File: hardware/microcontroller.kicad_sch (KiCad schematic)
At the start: 19 parts, among them U1 STM32G474QBT6

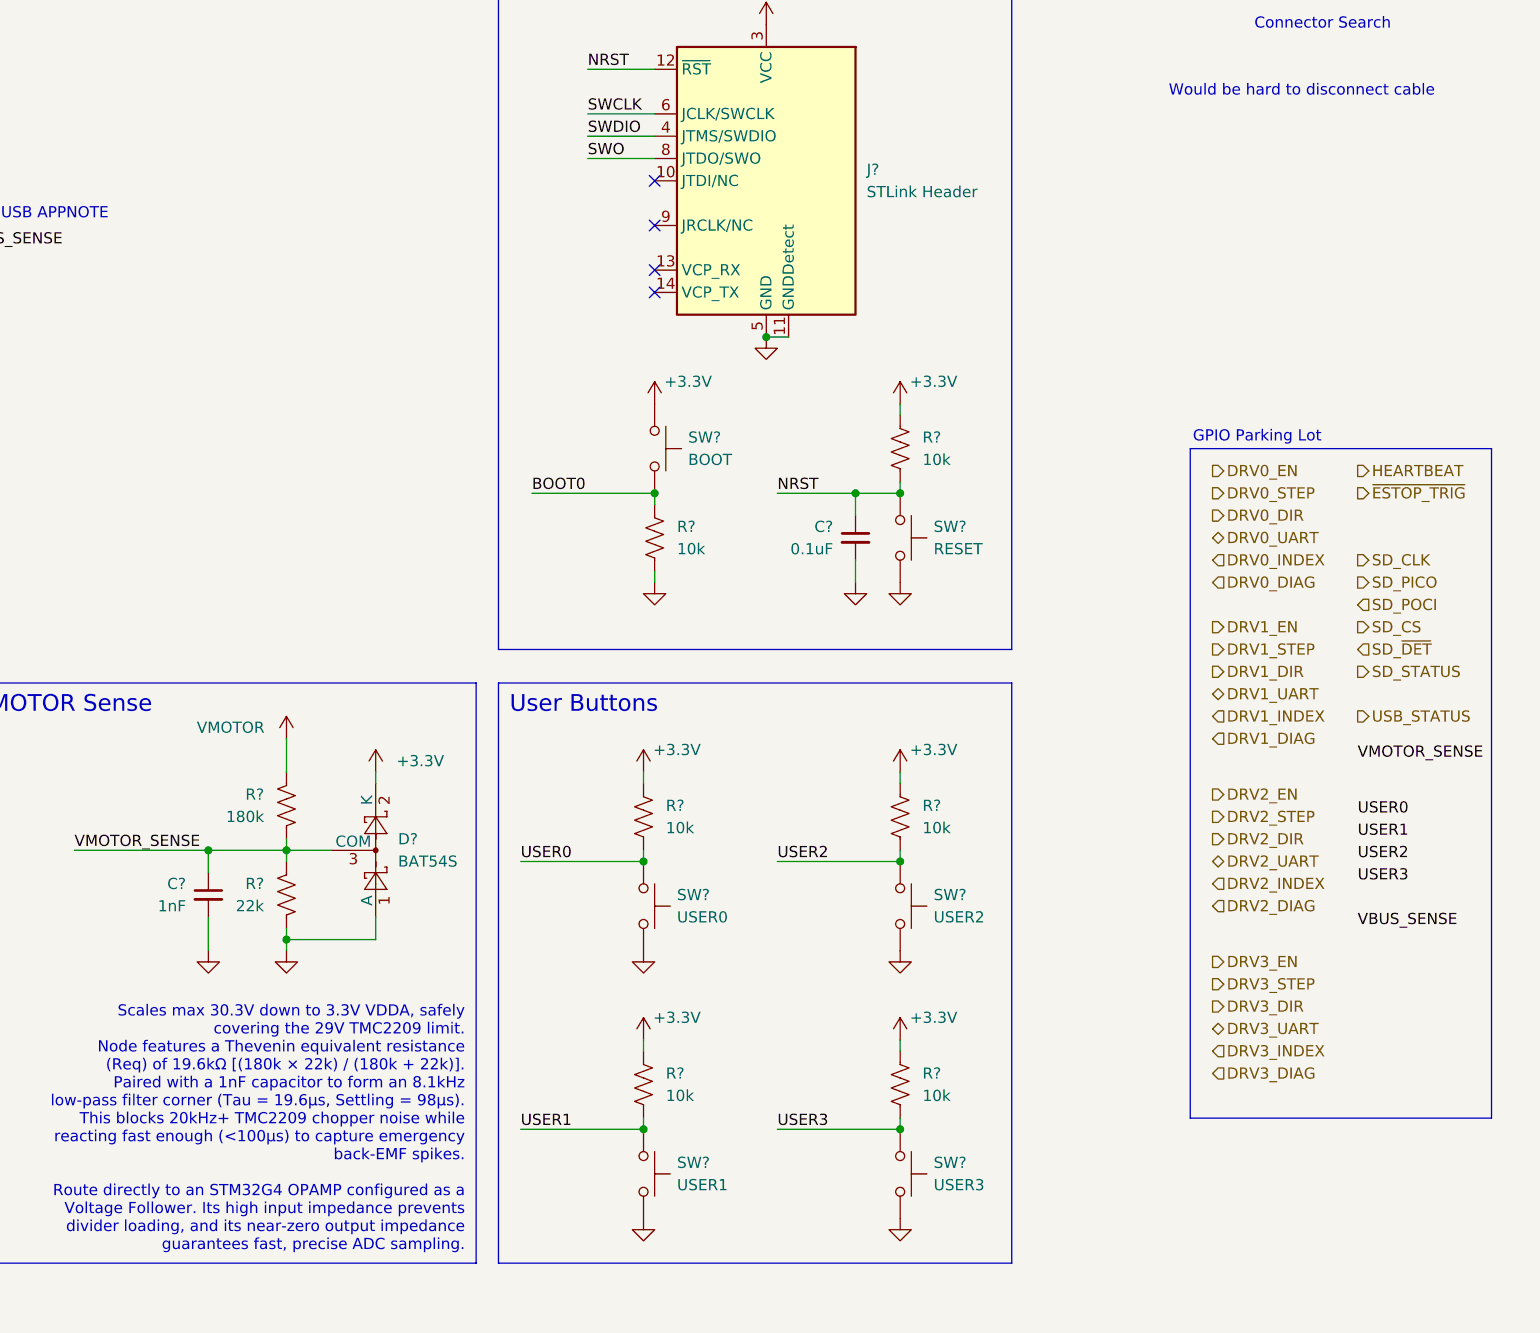
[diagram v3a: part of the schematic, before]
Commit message: Add QSPI Flash
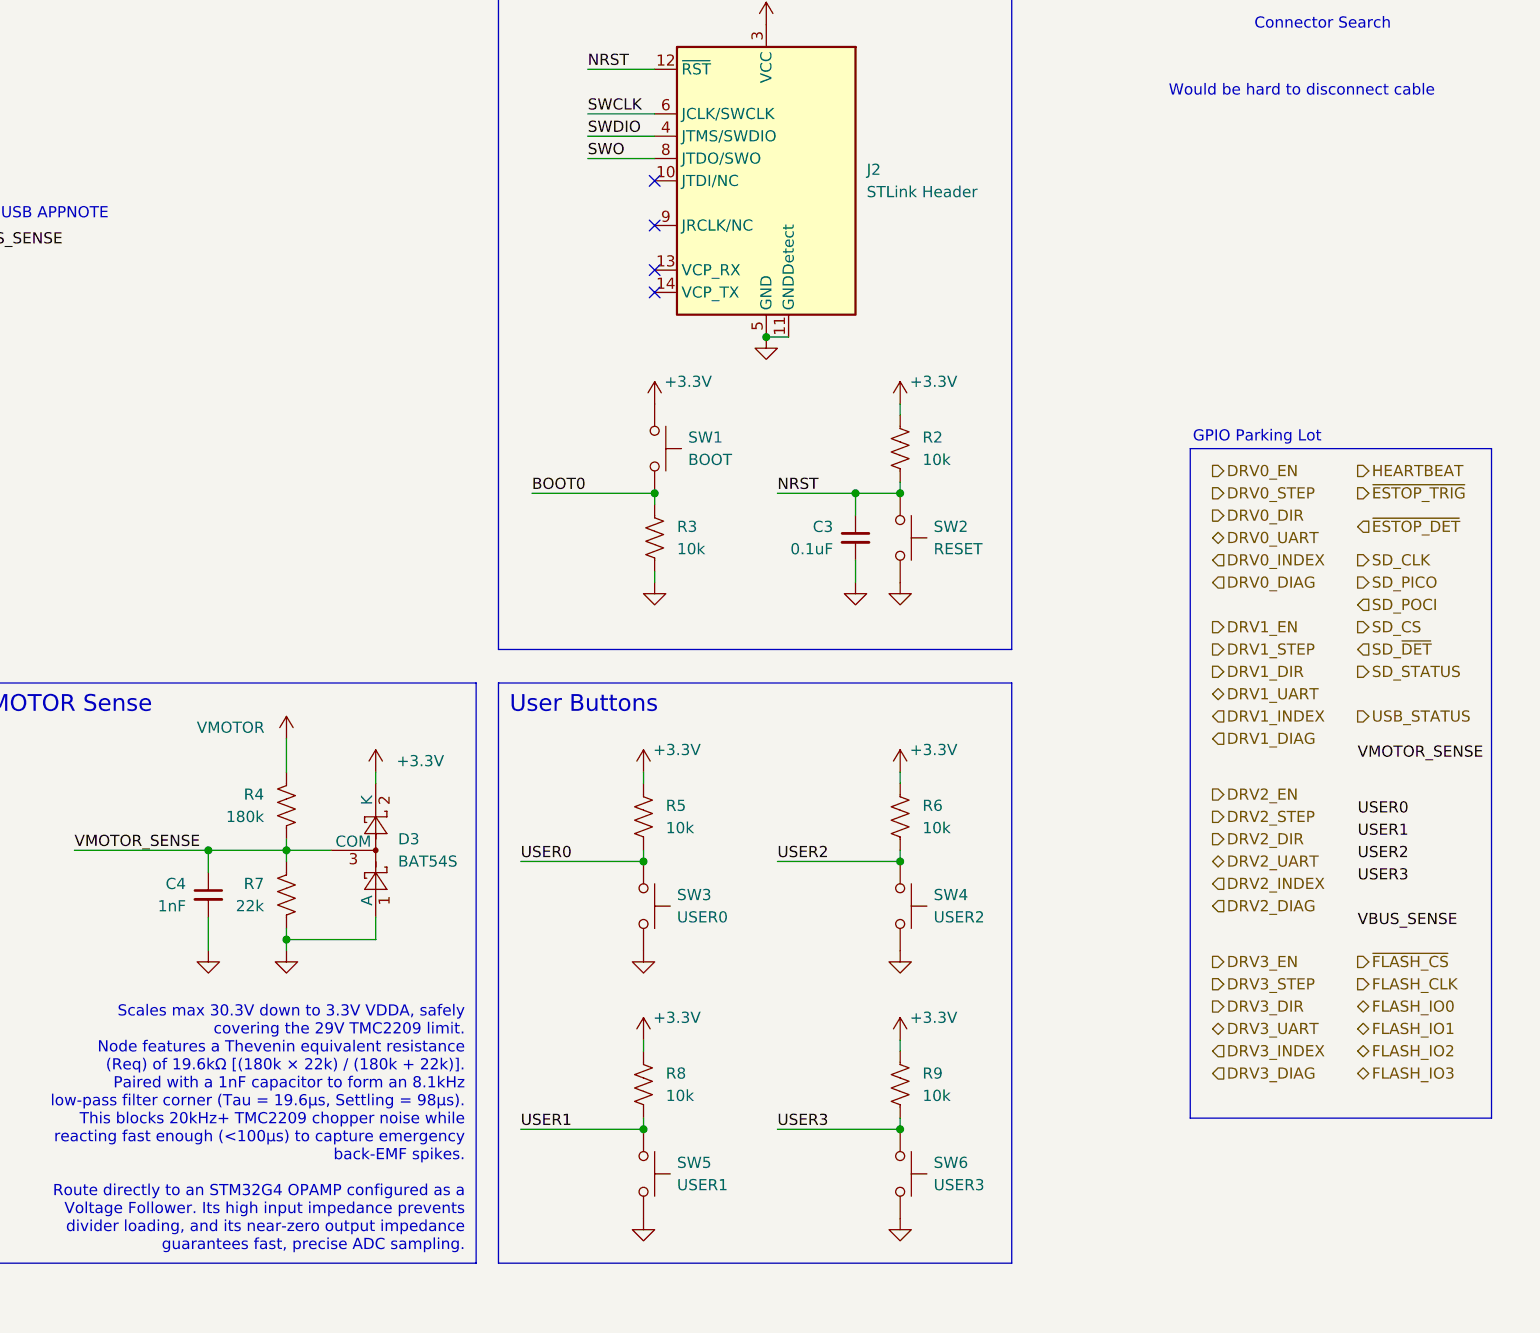
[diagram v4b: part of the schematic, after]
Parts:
- gave numbers to parts that had none: 18
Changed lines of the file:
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@@
 		)
 	)
+	(hierarchical_label "FLASH_CLK"
+		(shape output)
+		(at 303.53 137.16 0)
+		(fields_autoplaced yes)
+		(effects
+			(font
+				(size 1.27 1.27)
+			)
+			(justify left)
+		)
+		(property "GPIO Type" "QSPI"
+			(at 303.53 138.43 0)
+			(show_name no)
+			(do_not_autoplace no)
+			(effects
+				(font
+					(size 1.27 1.27)
+					(italic yes)
+				)
+				(justify left)
+			)
+		)
+	)
 	(hierarchical_label "DRV3_DIAG"
 		(shape input)
@@
 		)
 	)
+	(hierarchical_label "FLASH_IO2"
+		(shape bidirectional)
+		(at 303.53 144.78 0)
+		(fields_autoplaced yes)
+		(effects
+			(font
+				(size 1.27 1.27)
+			)
+			(justify left)
+		)
+		(property "GPIO Type" "QSPI"
+			(at 303.53 146.05 0)
+			(show_name no)
+			(do_not_autoplace no)
+			(effects
+				(font
+					(size 1.27 1.27)
+					(italic yes)
+				)
+				(justify left)
+			)
+		)
+	)
 	(hierarchical_label "DRV1_DIAG"
 		(shape input)
@@
 		)
 	)
+	(hierarchical_label "~{ESTOP_DET}"
+		(shape input)
+		(at 303.53 85.09 0)
+		(effects
+			(font
+				(size 1.27 1.27)
+			)
+			(justify left)
+		)
+	)
 	(hierarchical_label "USB_DP"
 		(shape input)
@@
 		)
 	)
+	(hierarchical_label "FLASH_IO0"
+		(shape bidirectional)
+		(at 303.53 139.7 0)
+		(fields_autoplaced yes)
+		(effects
+			(font
+				(size 1.27 1.27)
+			)
+			(justify left)
+		)
+		(property "GPIO Type" "QSPI"
+			(at 303.53 140.97 0)
+			(show_name no)
+			(do_not_autoplace no)
+			(effects
+				(font
+					(size 1.27 1.27)
+					(italic yes)
+				)
+				(justify left)
+			)
+		)
+	)
 	(hierarchical_label "DRV1_STEP"
 		(shape output)
@@
 		)
 	)
+	(hierarchical_label "FLASH_IO1"
+		(shape bidirectional)
+		(at 303.53 142.24 0)
+		(fields_autoplaced yes)
+		(effects
+			(font
+				(size 1.27 1.27)
+			)
+			(justify left)
+		)
+		(property "GPIO Type" "QSPI"
+			(at 303.53 143.51 0)
+			(show_name no)
+			(do_not_autoplace no)
+			(effects
+				(font
+					(size 1.27 1.27)
+					(italic yes)
+				)
+				(justify left)
+			)
+		)
+	)
 	(hierarchical_label "DRV3_DIR"
 		(shape output)
@@
 		)
 	)
+	(hierarchical_label "FLASH_IO3"
+		(shape bidirectional)
+		(at 303.53 147.32 0)
+		(fields_autoplaced yes)
+		(effects
+			(font
+				(size 1.27 1.27)
+			)
+			(justify left)
+		)
+		(property "GPIO Type" "QSPI"
+			(at 303.53 148.59 0)
+			(show_name no)
+			(do_not_autoplace no)
+			(effects
+				(font
+					(size 1.27 1.27)
+					(italic yes)
+				)
+				(justify left)
+			)
+		)
+	)
 	(hierarchical_label "DRV1_DIR"
 		(shape output)
@@
 		)
 	)
+	(hierarchical_label "~{FLASH_CS}"
+		(shape output)
+		(at 303.53 134.62 0)
+		(effects
+			(font
+				(size 1.27 1.27)
+			)
+			(justify left)
+		)
+	)
 	(hierarchical_label "SD_CS"
 		(shape output)
@@
 		(in_pos_files yes)
 		(dnp no)
-		(property "Reference" "C?"
+		(property "Reference" "C4"
 			(at 170.18 125.7362 0)
 			(show_name no)
@@
 			(project "stepping-stone"
 				(path "/793a882e-3f7b-468b-a863-41a1f527e1bf/d2f9d032-a5e5-45d0-b37f-4be86e3babb1"
-					(reference "C?")
+					(reference "C4")
 					(unit 1)
 				)
@@
 		(dnp no)
 		(fields_autoplaced yes)
-		(property "Reference" "R?"
+		(property "Reference" "R5"
 			(at 224.79 116.8399 0)
 			(show_name no)
@@
 			(project "stepping-stone"
 				(path "/793a882e-3f7b-468b-a863-41a1f527e1bf/d2f9d032-a5e5-45d0-b37f-4be86e3babb1"
-					(reference "R?")
+					(reference "R5")
 					(unit 1)
 				)
@@
 		(in_pos_files yes)
 		(dnp no)
-		(property "Reference" "R?"
+		(property "Reference" "R4"
 			(at 179.07 115.5699 0)
 			(show_name no)
@@
 			(project "stepping-stone"
 				(path "/793a882e-3f7b-468b-a863-41a1f527e1bf/d2f9d032-a5e5-45d0-b37f-4be86e3babb1"
-					(reference "R?")
+					(reference "R4")
 					(unit 1)
 				)
@@
 		(dnp no)
 		(fields_autoplaced yes)
-		(property "Reference" "R?"
+		(property "Reference" "R6"
 			(at 254 116.8399 0)
 			(show_name no)
@@
 			(project "stepping-stone"
 				(path "/793a882e-3f7b-468b-a863-41a1f527e1bf/d2f9d032-a5e5-45d0-b37f-4be86e3babb1"
-					(reference "R?")
+					(reference "R6")
 					(unit 1)
 				)
@@
 		(in_pos_files yes)
 		(dnp no)
-		(property "Reference" "R?"
+		(property "Reference" "R7"
 			(at 179.07 125.7299 0)
 			(show_name no)
@@
 			(project "stepping-stone"
 				(path "/793a882e-3f7b-468b-a863-41a1f527e1bf/d2f9d032-a5e5-45d0-b37f-4be86e3babb1"
-					(reference "R?")
+					(reference "R7")
 					(unit 1)
 				)
@@
 		(dnp no)
 		(fields_autoplaced yes)
-		(property "Reference" "J?"
+		(property "Reference" "J2"
 			(at 247.65 44.4499 0)
 			(show_name no)
@@
 			(project "stepping-stone"
 				(path "/793a882e-3f7b-468b-a863-41a1f527e1bf/d2f9d032-a5e5-45d0-b37f-4be86e3babb1"
-					(reference "J?")
+					(reference "J2")
 					(unit 1)
 				)
@@
 		(in_pos_files yes)
 		(dnp no)
-		(property "Reference" "SW?"
+		(property "Reference" "SW6"
 			(at 255.27 157.48 90)
 			(show_name no)
@@
 			(project "stepping-stone"
 				(path "/793a882e-3f7b-468b-a863-41a1f527e1bf/d2f9d032-a5e5-45d0-b37f-4be86e3babb1"
-					(reference "SW?")
+					(reference "SW6")
 					(unit 1)
 				)
@@
 		(in_pos_files yes)
 		(dnp no)
-		(property "Reference" "SW?"
+		(property "Reference" "SW5"
 			(at 226.06 157.48 90)
 			(show_name no)
@@
 			(project "stepping-stone"
 				(path "/793a882e-3f7b-468b-a863-41a1f527e1bf/d2f9d032-a5e5-45d0-b37f-4be86e3babb1"
-					(reference "SW?")
+					(reference "SW5")
 					(unit 1)
 				)
@@
 		(dnp no)
 		(fields_autoplaced yes)
-		(property "Reference" "D?"
+		(property "Reference" "D3"
 			(at 194.31 120.6499 90)
 			(show_name no)
@@
 			(project "stepping-stone"
 				(path "/793a882e-3f7b-468b-a863-41a1f527e1bf/d2f9d032-a5e5-45d0-b37f-4be86e3babb1"
-					(reference "D?")
+					(reference "D3")
 					(unit 1)
 				)
@@
 		(in_pos_files yes)
 		(dnp no)
-		(property "Reference" "SW?"
+		(property "Reference" "SW3"
 			(at 226.06 127 90)
 			(show_name no)
@@
 			(project "stepping-stone"
 				(path "/793a882e-3f7b-468b-a863-41a1f527e1bf/d2f9d032-a5e5-45d0-b37f-4be86e3babb1"
-					(reference "SW?")
+					(reference "SW3")
 					(unit 1)
 				)
@@
 		(dnp no)
 		(fields_autoplaced yes)
-		(property "Reference" "R?"
+		(property "Reference" "R2"
 			(at 254 74.9299 0)
 			(show_name no)
@@
 			(project "stepping-stone"
 				(path "/793a882e-3f7b-468b-a863-41a1f527e1bf/d2f9d032-a5e5-45d0-b37f-4be86e3babb1"
-					(reference "R?")
+					(reference "R2")
 					(unit 1)
 				)
@@
 		(in_pos_files yes)
 		(dnp no)
-		(property "Reference" "SW?"
+		(property "Reference" "SW1"
 			(at 227.33 74.93 90)
 			(show_name no)
@@
 			(project "stepping-stone"
 				(path "/793a882e-3f7b-468b-a863-41a1f527e1bf/d2f9d032-a5e5-45d0-b37f-4be86e3babb1"
-					(reference "SW?")
+					(reference "SW1")
 					(unit 1)
 				)
@@
 		(dnp no)
 		(fields_autoplaced yes)
-		(property "Reference" "R?"
+		(property "Reference" "R8"
 			(at 224.79 147.3199 0)
 			(show_name no)
@@
 			(project "stepping-stone"
 				(path "/793a882e-3f7b-468b-a863-41a1f527e1bf/d2f9d032-a5e5-45d0-b37f-4be86e3babb1"
-					(reference "R?")
+					(reference "R8")
 					(unit 1)
 				)
@@
 		(in_pos_files yes)
 		(dnp no)
-		(property "Reference" "SW?"
+		(property "Reference" "SW4"
 			(at 255.27 127 90)
 			(show_name no)
@@
 			(project "stepping-stone"
 				(path "/793a882e-3f7b-468b-a863-41a1f527e1bf/d2f9d032-a5e5-45d0-b37f-4be86e3babb1"
-					(reference "SW?")
+					(reference "SW4")
 					(unit 1)
 				)
@@
 		(in_pos_files yes)
 		(dnp no)
-		(property "Reference" "SW?"
+		(property "Reference" "SW2"
 			(at 255.27 85.09 90)
 			(show_name no)
@@
 			(project "stepping-stone"
 				(path "/793a882e-3f7b-468b-a863-41a1f527e1bf/d2f9d032-a5e5-45d0-b37f-4be86e3babb1"
-					(reference "SW?")
+					(reference "SW2")
 					(unit 1)
 				)
@@
 		(in_pos_files yes)
 		(dnp no)
-		(property "Reference" "C?"
+		(property "Reference" "C3"
 			(at 243.84 85.0962 0)
 			(show_name no)
@@
 			(project "stepping-stone"
 				(path "/793a882e-3f7b-468b-a863-41a1f527e1bf/d2f9d032-a5e5-45d0-b37f-4be86e3babb1"
-					(reference "C?")
+					(reference "C3")
 					(unit 1)
 				)
@@
 		(dnp no)
 		(fields_autoplaced yes)
-		(property "Reference" "R?"
+		(property "Reference" "R3"
 			(at 226.06 85.0899 0)
 			(show_name no)
@@
 			(project "stepping-stone"
 				(path "/793a882e-3f7b-468b-a863-41a1f527e1bf/d2f9d032-a5e5-45d0-b37f-4be86e3babb1"
-					(reference "R?")
+					(reference "R3")
 					(unit 1)
 				)
@@
 		(dnp no)
 		(fields_autoplaced yes)
-		(property "Reference" "R?"
+		(property "Reference" "R9"
 			(at 254 147.3199 0)
 			(show_name no)
@@
 			(project "stepping-stone"
 				(path "/793a882e-3f7b-468b-a863-41a1f527e1bf/d2f9d032-a5e5-45d0-b37f-4be86e3babb1"
-					(reference "R?")
+					(reference "R9")
 					(unit 1)
 				)

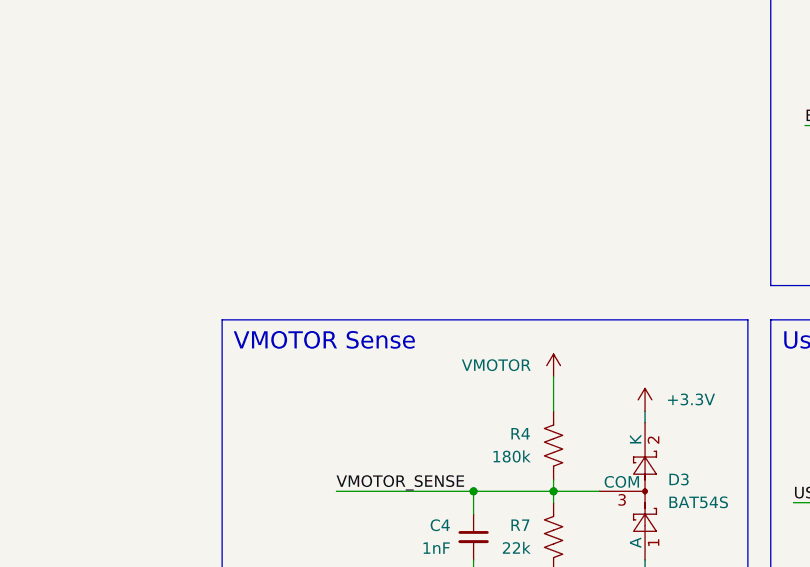
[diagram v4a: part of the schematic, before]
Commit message: Adjust power input protection
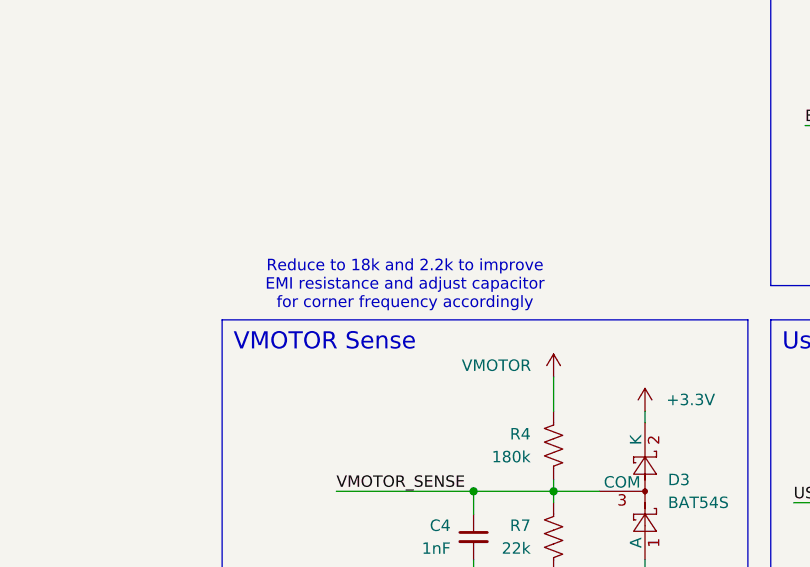
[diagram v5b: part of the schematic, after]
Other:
- note added: "Reduce to 18k and 2.2k to improve EMI resistance and adjust capacitor for corner frequency accordingly"
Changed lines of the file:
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@@
+		)
+	)
+	(text "Reduce to 18k and 2.2k to improve\nEMI resistance and adjust capacitor\nfor corner frequency accordingly"
+		(exclude_from_sim no)
+		(at 165.1 99.06 0)
+		(effects
+			(font
+				(size 1.27 1.27)
+				(color 132 0 0 1)
+			)
 		)
 	)

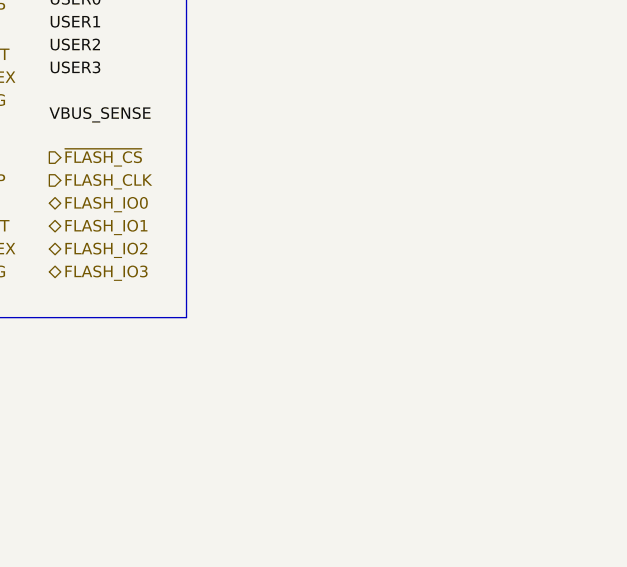
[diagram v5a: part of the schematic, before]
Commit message: Added Limit Switch Page
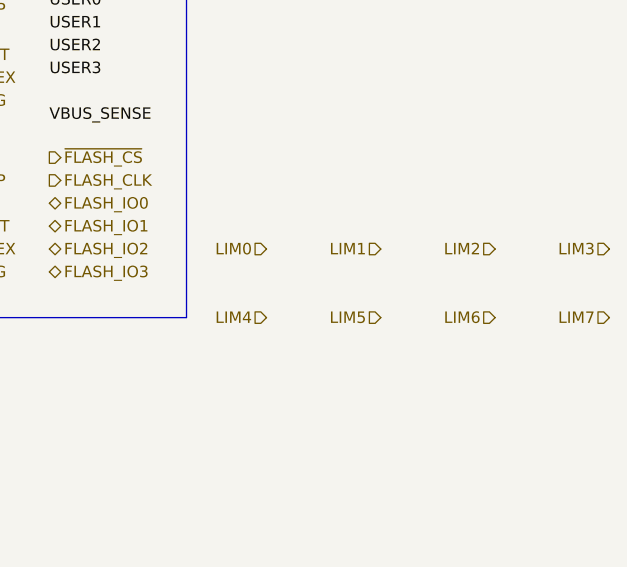
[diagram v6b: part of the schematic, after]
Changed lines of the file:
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@@
+		)
+	)
+	(hierarchical_label "LIM6"
+		(shape input)
+		(at 353.06 152.4 180)
+		(effects
+			(font
+				(size 1.27 1.27)
+			)
+			(justify right)
 		)
 	)
@@
 		)
 	)
+	(hierarchical_label "LIM2"
+		(shape input)
+		(at 353.06 144.78 180)
+		(effects
+			(font
+				(size 1.27 1.27)
+			)
+			(justify right)
+		)
+	)
 	(hierarchical_label "DRV2_DIAG"
 		(shape input)
@@
 		)
 	)
+	(hierarchical_label "LIM5"
+		(shape input)
+		(at 340.36 152.4 180)
+		(effects
+			(font
+				(size 1.27 1.27)
+			)
+			(justify right)
+		)
+	)
 	(hierarchical_label "FLASH_IO3"
 		(shape bidirectional)
@@
 		)
 	)
+	(hierarchical_label "LIM7"
+		(shape input)
+		(at 365.76 152.4 180)
+		(effects
+			(font
+				(size 1.27 1.27)
+			)
+			(justify right)
+		)
+	)
 	(hierarchical_label "USB_STATUS"
 		(shape output)
@@
 		)
 	)
+	(hierarchical_label "LIM4"
+		(shape input)
+		(at 327.66 152.4 180)
+		(effects
+			(font
+				(size 1.27 1.27)
+			)
+			(justify right)
+		)
+	)
+	(hierarchical_label "LIM0"
+		(shape input)
+		(at 327.66 144.78 180)
+		(effects
+			(font
+				(size 1.27 1.27)
+			)
+			(justify right)
+		)
+	)
+	(hierarchical_label "LIM1"
+		(shape input)
+		(at 340.36 144.78 180)
+		(effects
+			(font
+				(size 1.27 1.27)
+			)
+			(justify right)
+		)
+	)
 	(hierarchical_label "SD_CS"
 		(shape output)
@@
 		)
 	)
+	(hierarchical_label "LIM3"
+		(shape input)
+		(at 365.76 144.78 180)
+		(effects
+			(font
+				(size 1.27 1.27)
+			)
+			(justify right)
+		)
+	)
